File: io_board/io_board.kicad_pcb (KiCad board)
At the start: 2 copper layers, 80 x 100 mm, 83 parts, among them J10 RST1, J11 D1, J12 Osc2, J13 Rung2, J14 Sin2, J15 Gate2, J16 Ring, J18 RST2, J19 D2, J21 CV1, J22 CV2, J4 STRB1, J5 STRB2, J6 Osc1, J7 Sin1, J8 Rung1, J9 Gate1, Q1 2N3904, Q10 2N3904, Q11 2N3904, Q2 2N3904, Q5 2N3904, Q6 2N3904, Q7 2N3904, Q8 2N3904, Q9 2N3904, SW1 SW_SPDT, U3 TL074

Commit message: Routing done, panel done
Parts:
- moved R41 16.3 mm to (33.2, 41.7)
- moved Q11 9.01 mm to (41.3, 51.6), turned to 180 degrees
- moved R42 8.30 mm to (47.2, 40.6), turned to -90 degrees
- moved R49 7.82 mm to (64.1, 67.0), turned to 180 degrees
- moved R38 7.82 mm to (16.0, 67.0), turned to 0 degrees
- moved D2 6.75 mm to (58.8, 26.5)
- moved D1 6.50 mm to (18.7, 26.5)
- moved Q1 6.11 mm to (18.5, 34.1)
- moved R25 5.77 mm to (67.0, 31.9)
- moved Q2 4.86 mm to (61.5, 32.1), turned to 180 degrees
- moved R54 4.50 mm to (43.9, 1.75)
- moved R20 3.82 mm to (14.5, 30.2)
- moved D9 3.57 mm to (48.5, 19.6), turned to 90 degrees
- moved D10 3.51 mm to (48.5, 23.2), turned to -90 degrees
- moved R50 3.38 mm to (44.2, 48.2)
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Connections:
- J17 pad 3: Rst1 -> unconnected-(J17-Pad3)
- J17 pad 4: D1 -> RM
- J17 pad 5: unconnected-(J17-Pad5) -> D1
- J17 pad 6: RM -> Osc1
- J17 pad 7: Osc1 -> Rst1
- J20 pad 10: Sin2 -> Rung2
- J20 pad 11: Rung2 -> Sin2
- J20 pad 3: Rst2 -> Osc3sw
- J20 pad 5: Osc3sw -> Osc2
- J20 pad 7: Osc2 -> Clk2
- J20 pad 8: Clk2 -> QB8
- J20 pad 9: QB8 -> Rst2
- U3 pad 10: Net-(R57-Pad1) -> Net-(R58-Pad1)
- U3 pad 12: Net-(R58-Pad1) -> Net-(R57-Pad1)
- U3 pad 14: Net-(D10-Pad2) -> Net-(D9-Pad2)
- U3 pad 8: Net-(D9-Pad2) -> Net-(D10-Pad2)
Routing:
- net 12v: track 0.00 -> 286.6 mm
- net -12v: track 0.00 -> 77.9 mm
- net Rst2: track 0.00 -> 57.2 mm
- net Net-(R58-Pad1): track 0.00 -> 57.1 mm
- net Net-(R52-Pad1): track 0.00 -> 53.8 mm
- net Rst1: track 0.00 -> 52.3 mm
- net Net-(R57-Pad1): track 0.00 -> 49.2 mm
- net Net-(R51-Pad1): track 0.00 -> 46.8 mm
- net Sin2: track 0.00 -> 46.2 mm
- net Net-(J9-PadT): track 0.00 -> 45.9 mm
- net Net-(J15-PadT): track 0.00 -> 45.0 mm
- net D1: track 0.00 -> 44.9 mm
- net Osc3sw: track 0.00 -> 44.6 mm
- net Net-(FREQ1-Pad2): track 0.00 -> 44.5 mm, vias 0 -> 1
- net Net-(FREQ2-Pad2): track 0.00 -> 44.2 mm
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- added copper zone on B.Cu, net GND
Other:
- outline, holes or cut-outs redrawn

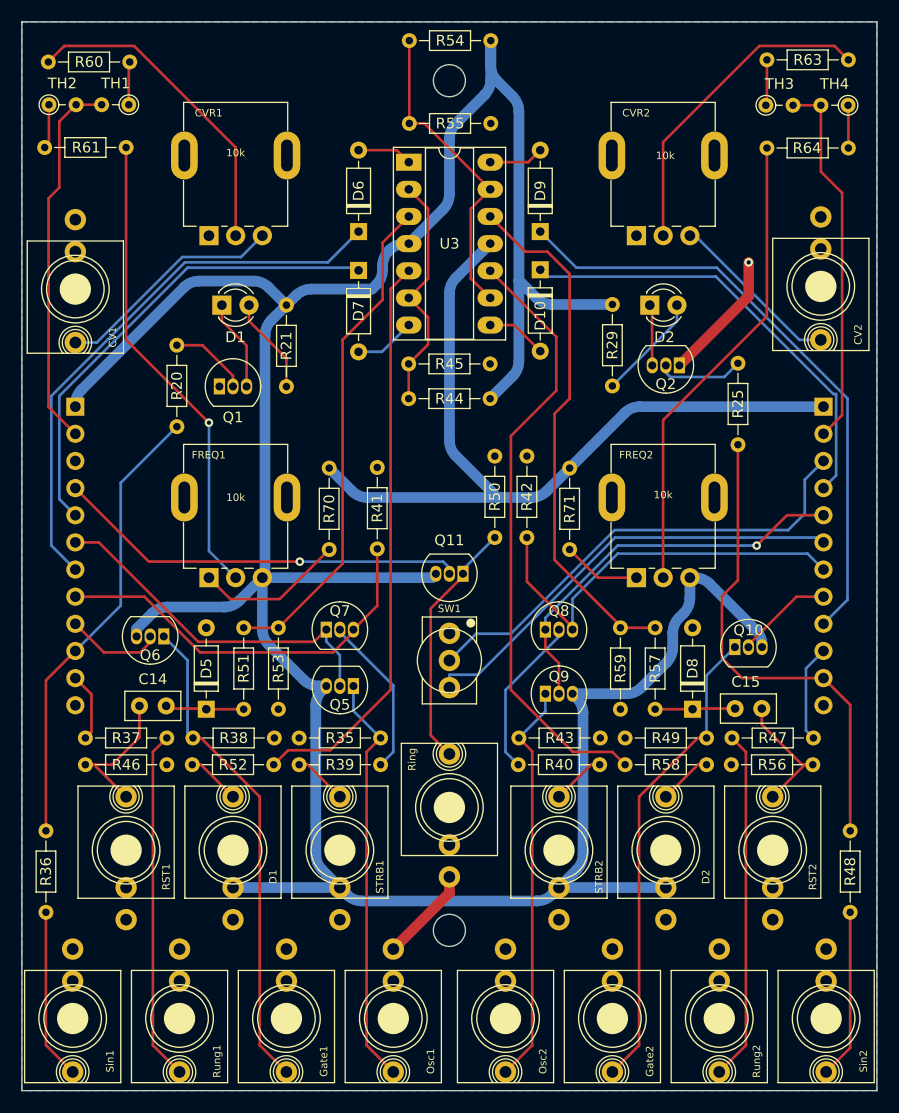
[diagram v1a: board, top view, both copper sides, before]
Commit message: Rejigged layout for more space
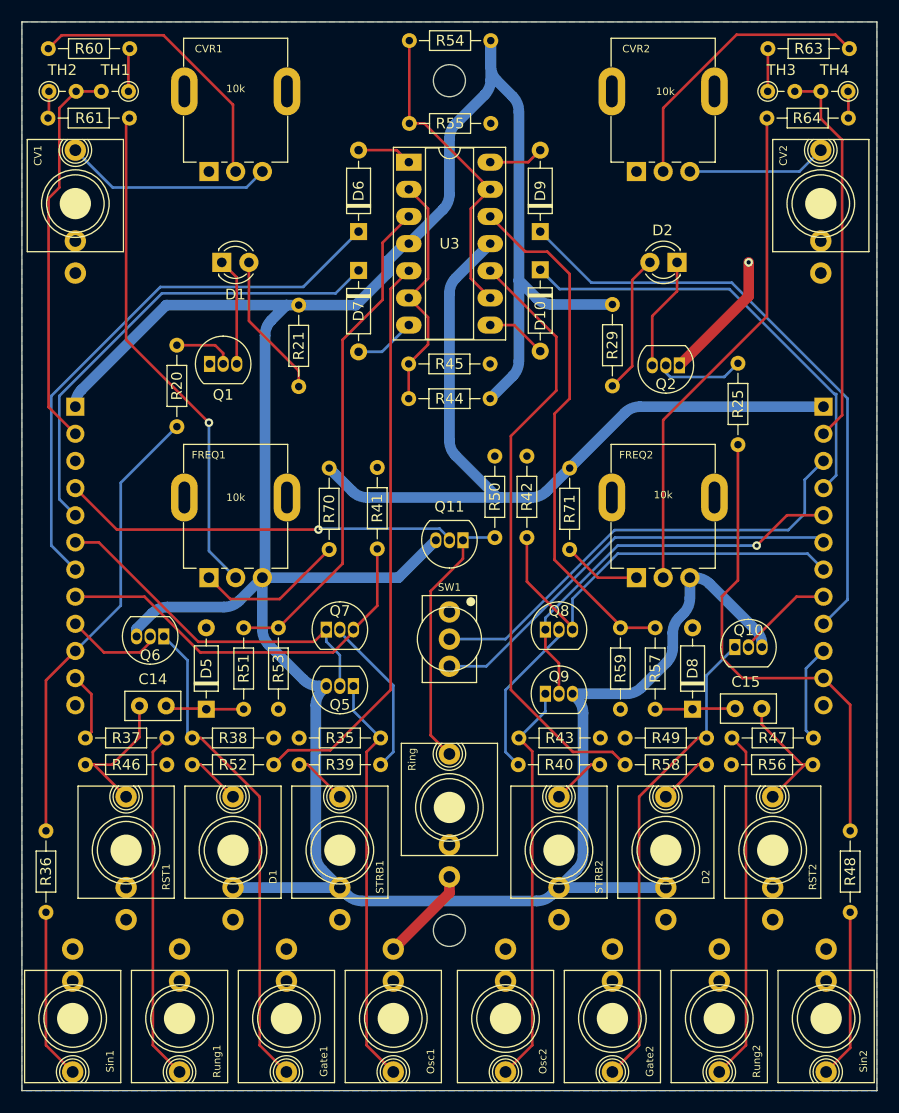
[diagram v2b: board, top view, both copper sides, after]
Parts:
- moved J21 8.00 mm to (5.00, 17.0), turned to 0 degrees
- moved J22 7.75 mm to (74.8, 17.0), turned to 0 degrees
- moved CVR1 6.00 mm to (20.0, 6.50)
- moved CVR2 6.00 mm to (60.0, 6.50)
- moved D2 4.74 mm to (61.3, 22.5), turned to 180 degrees
- moved D1 4.00 mm to (18.7, 22.5)
- moved Q11 3.14 mm to (41.3, 48.5)
- moved R64 2.80 mm to (69.7, 9.00)
- moved R61 2.77 mm to (10.1, 9.00)
- moved Q1 2.30 mm to (17.6, 32.0)
- moved SW1 2.00 mm to (40.0, 57.8)
- moved TH3 1.31 mm to (69.8, 6.50)
- moved TH4 1.30 mm to (77.3, 6.50)
- moved TH1 1.25 mm to (9.97, 6.50)
- moved R60 1.25 mm to (2.47, 2.50)
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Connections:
- CVR1 pad : (no net) -> GND
- FREQ1 pad : (no net) -> GND
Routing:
- net Net-(D2-Pad1): track 5.74 -> 10.6 mm
- net Net-(D1-Pad2): track 9.07 -> 13.6 mm
- net Net-(CVR2-Pad2): track 30.3 -> 26.7 mm
- net Net-(CVR1-Pad2): track 30.3 -> 26.7 mm
- net Net-(CVR2-Pad3): track 16.3 -> 13.1 mm
- net Net-(D2-Pad2): track 10.1 -> 13.0 mm
- net Net-(FREQ1-Pad2): track 44.5 -> 47.4 mm
- net Net-(FREQ2-Pad2): track 44.2 -> 47.0 mm
- net Net-(CVR1-Pad3): track 21.6 -> 19.6 mm
- net Net-(Q1-Pad2): track 7.43 -> 5.64 mm
- net RM: track 38.6 -> 37.0 mm
- net Net-(J16-PadT): track 23.5 -> 25.1 mm
- net Net-(R61-Pad2): track 4.17 -> 2.62 mm
- net Osc3: track 41.7 -> 40.2 mm
- net Net-(D1-Pad1): track 8.57 -> 10.1 mm
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
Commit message: Updates to panel etc.
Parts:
- added R72: 100k, Resistor_THT:R_Axial_DIN0204_L3.6mm_D1.6mm_P7.62mm_Horizontal, F.Cu at (13.5, 26.5)
- added R73: 22k, Resistor_THT:R_Axial_DIN0204_L3.6mm_D1.6mm_P7.62mm_Horizontal, F.Cu at (16.2, 17.2)
- added R74: 100k, Resistor_THT:R_Axial_DIN0204_L3.6mm_D1.6mm_P7.62mm_Horizontal, F.Cu at (53.0, 26.5)
- added R75: 22k, Resistor_THT:R_Axial_DIN0204_L3.6mm_D1.6mm_P7.62mm_Horizontal, F.Cu at (56.2, 17.2)
- moved R25 1.50 mm to (68.5, 31.9)
- moved R20 1.00 mm to (13.5, 30.2)
- moved R29 0.25 mm to (55.5, 26.4)
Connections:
- CVR1 pad : GND -> (no net)
- FREQ1 pad : GND -> (no net)
- J21 pad TN: unconnected-(J21-PadTN) -> Net-(J21-PadTN)
- J22 pad TN: unconnected-(J22-PadTN) -> Net-(J22-PadTN)
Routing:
- net Net-(J22-PadTN): track 0.00 -> 23.8 mm
- net Net-(J21-PadTN): track 0.00 -> 12.5 mm
- net Net-(Q2-Pad2): track 8.13 -> 9.63 mm
- net Net-(Q1-Pad2): track 5.64 -> 6.64 mm
- net Sin2: track 46.2 -> 46.8 mm

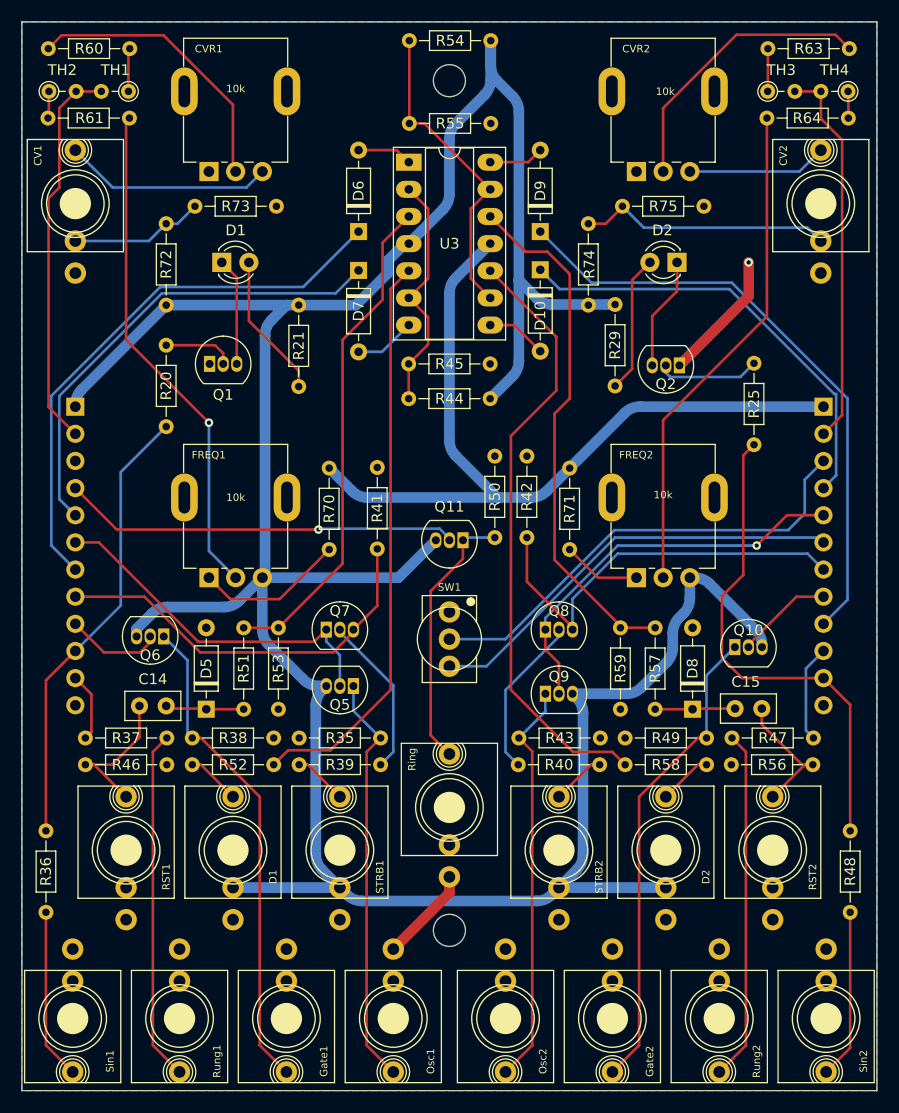
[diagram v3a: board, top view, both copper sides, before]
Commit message: Removed the unneccessary 100ohm resistor after the expo converter
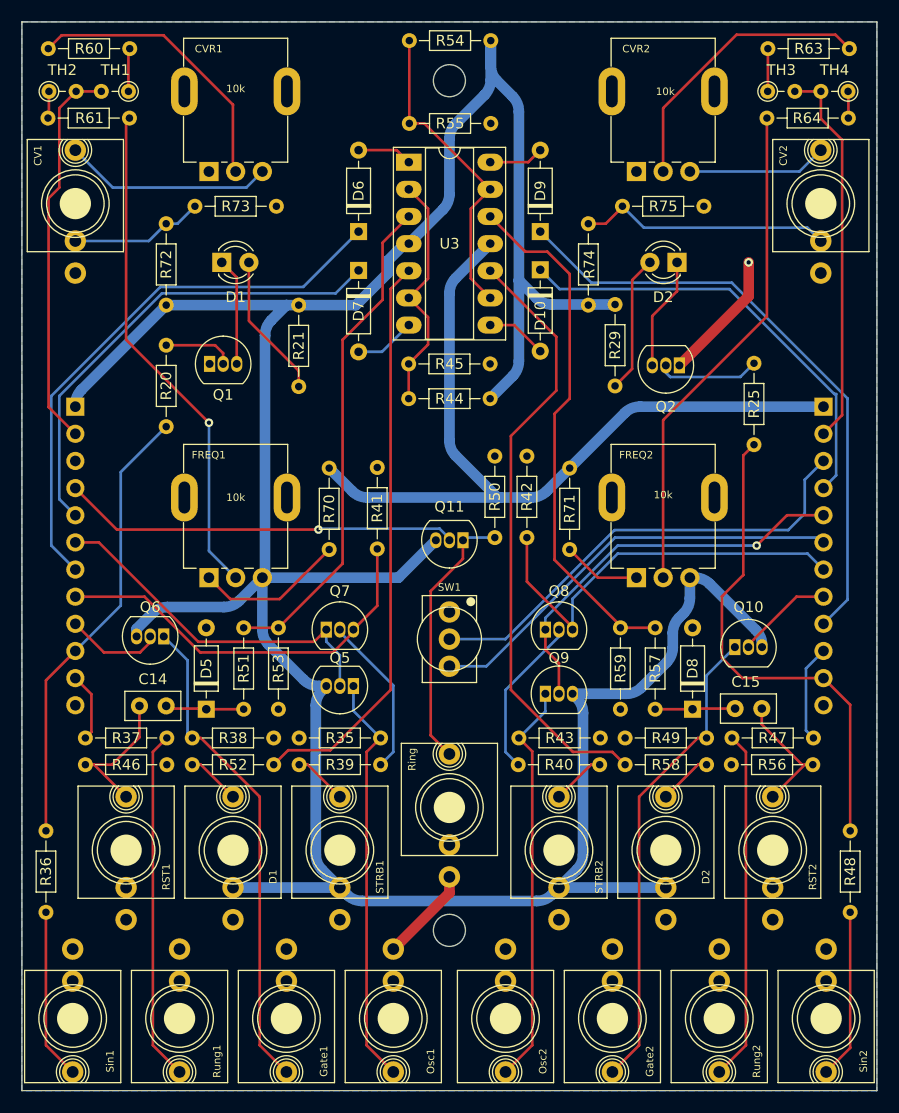
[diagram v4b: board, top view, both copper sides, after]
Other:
- board text added: "Dual Digital Sine Wave Generator Design and PCB by Neil Massey CC-BY-NC-SA 3.0 (2022) Rev 0"
- board text removed: "Design and PCB by Neil Massey CC-BY-NC-SA 3.0 (2022) Rev 0"
- board text removed: "Dual Digital Sine Wave Generator"
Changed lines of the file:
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@@
     (pad_to_mask_clearance 0)
     (pcbplotparams
-      (layerselection 0x0080000_7ffffffe)
+      (layerselection 0x00010fc_ffffffff)
       (disableapertmacros false)
-      (usegerberextensions false)
-      (usegerberattributes true)
-      (usegerberadvancedattributes true)
+      (usegerberextensions true)
+      (usegerberattributes false)
+      (usegerberadvancedattributes false)
       (creategerberjobfile true)
       (svguseinch false)
@@
       (psnegative false)
       (psa4output false)
-      (plotreference false)
+      (plotreference true)
       (plotvalue false)
       (plotinvisibletext false)
       (sketchpadsonfab false)
-      (subtractmaskfromsilk false)
-      (outputformat 3)
+      (subtractmaskfromsilk true)
+      (outputformat 1)
       (mirror false)
       (drillshape 0)
       (scaleselection 1)
-      (outputdirectory "../Assets/")
+      (outputdirectory "gerbers/")
     )
   )
@@
     (property "Sheetname" "")
     (attr through_hole)
-    (fp_text reference "Q2" (at 1.27 -1.75 180) (layer "F.SilkS")
+    (fp_text reference "Q2" (at 1.27 -3.86 180) (layer "F.SilkS")
       (effects (font (size 1 1) (thickness 0.15)))
     )
@@
     (property "Sheetname" "")
     (attr through_hole)
-    (fp_text reference "D2" (at 1.366487 3) (layer "F.SilkS")
+    (fp_text reference "D2" (at 1.3 -3.25) (layer "F.SilkS")
       (effects (font (size 1 1) (thickness 0.15)))
     )
@@
     (property "Sheetname" "")
     (attr through_hole)
-    (fp_text reference "Q10" (at 1.27 -1.58) (layer "F.SilkS")
+    (fp_text reference "Q10" (at 1.27 -3.75) (layer "F.SilkS")
       (effects (font (size 1 1) (thickness 0.15)))
     )
@@
     (property "Sheetname" "")
     (attr through_hole)
-    (fp_text reference "Q6" (at 1.27 -1.75) (layer "F.SilkS")
+    (fp_text reference "Q6" (at 1.27 2.75) (layer "F.SilkS")
       (effects (font (size 1 1) (thickness 0.15)))
     )
@@
     (property "Sheetname" "")
     (attr through_hole)
-    (fp_text reference "Q5" (at 1.27 -1.75) (layer "F.SilkS")
+    (fp_text reference "Q5" (at 1.27 2.64) (layer "F.SilkS")
       (effects (font (size 1 1) (thickness 0.15)))
     )
@@
     (property "Sheetname" "")
     (attr through_hole)
-    (fp_text reference "Q7" (at 1.27 -1.75) (layer "F.SilkS")
+    (fp_text reference "Q7" (at 1.27 -3.61) (layer "F.SilkS")
       (effects (font (size 1 1) (thickness 0.15)))
     )
@@
     (property "Sheetname" "")
     (attr through_hole)
-    (fp_text reference "D1" (at 1.3 -3) (layer "F.SilkS")
+    (fp_text reference "D1" (at 1.3 3.25) (layer "F.SilkS")
       (effects (font (size 1 1) (thickness 0.15)))
     )
@@
     (property "Sheetname" "")
     (attr through_hole)
-    (fp_text reference "Q9" (at 1.27 -1.61) (layer "F.SilkS")
+    (fp_text reference "Q9" (at 1.27 -3.36) (layer "F.SilkS")
       (effects (font (size 1 1) (thickness 0.15)))
     )
@@
     (property "Sheetname" "")
     (attr through_hole)
-    (fp_text reference "Q8" (at 1.27 -1.75) (layer "F.SilkS")
+    (fp_text reference "Q8" (at 1.27 -3.61) (layer "F.SilkS")
       (effects (font (size 1 1) (thickness 0.15)))
     )
@@
   (gr_circle (center 74.75 17) (end 77.95 17) (layer "User.2") (width 0.15) (fill none))
   (gr_circle (center 60 6.5) (end 63.6 6.5) (layer "User.2") (width 0.15) (fill none))
-  (gr_text "DDSWG" (at 40.75 49.5 90) (layer "B.SilkS")
-    (effects (font (size 20 20) (thickness 3)) (justify mirror))
+  (gr_text "DDSWG" (at 73.5 83.25 90) (layer "B.SilkS")
+    (effects (font (size 5 5) (thickness 1)) (justify mirror))
   )
-  (gr_text "Design and PCB by Neil Massey\nCC-BY-NC-SA 3.0 (2022)\nRev 0" (at 16.5 27.5 90) (layer "B.SilkS")
-    (effects (font (size 2 2) (thickness 0.4)) (justify mirror))
-  )
-  (gr_text "Dual Digital Sine Wave Generator" (at 69.5 50 90) (layer "B.SilkS")
-    (effects (font (size 3.5 3.5) (thickness 0.5)) (justify mirror))
+  (gr_text "Dual Digital Sine Wave Generator\nDesign and PCB by Neil Massey\nCC-BY-NC-SA 3.0 (2022)\nRev 0" (at 7.5 83.5 90) (layer "B.SilkS")
+    (effects (font (size 1.2 1.2) (thickness 0.2)) (justify mirror))
   )
   (segment (start 13.5 64.25) (end 17.19 64.25) (width 0.25) (layer "F.Cu") (net 1))

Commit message: Added negative CV protection diodes
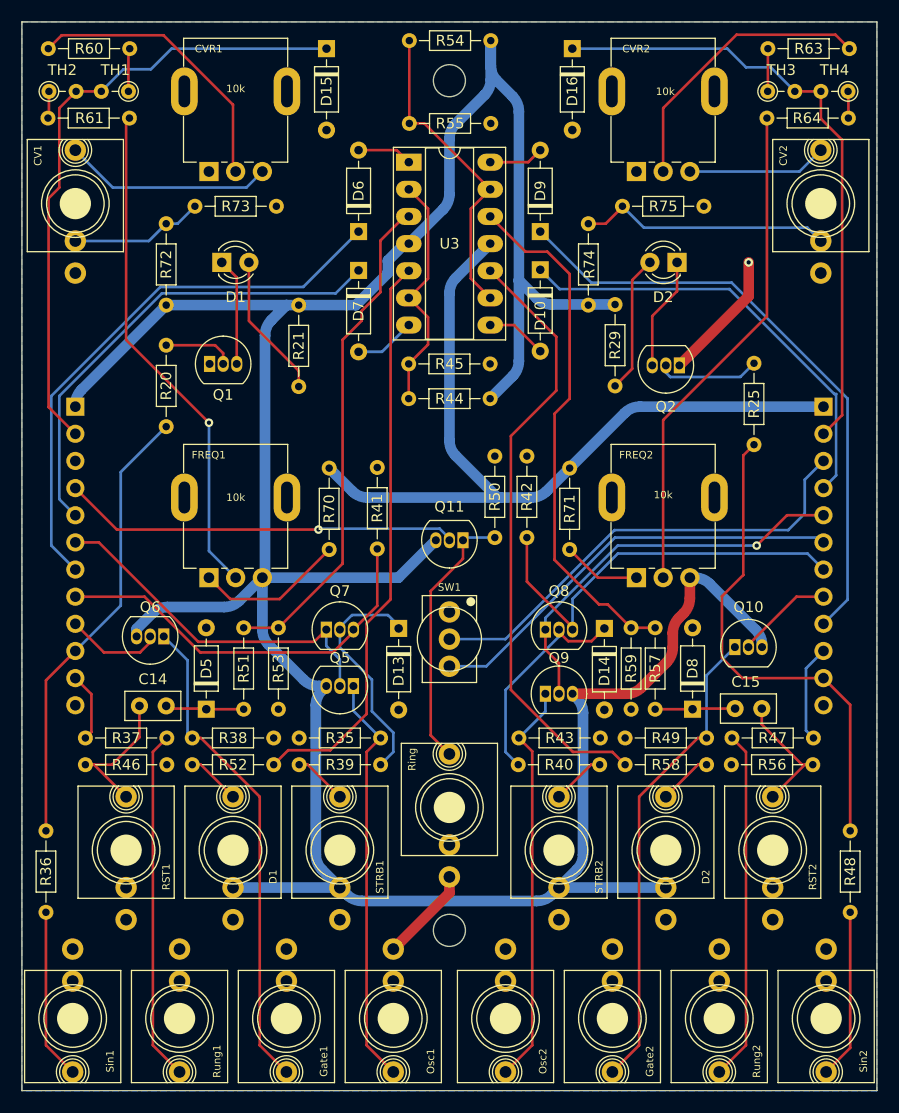
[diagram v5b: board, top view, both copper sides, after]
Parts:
- added D13: BAT42, Diode_THT:D_DO-35_SOD27_P7.62mm_Horizontal, F.Cu at (35.2, 56.8)
- added D14: BAT42, Diode_THT:D_DO-35_SOD27_P7.62mm_Horizontal, F.Cu at (54.5, 56.8)
- added D15: BAT42, Diode_THT:D_DO-35_SOD27_P7.62mm_Horizontal, F.Cu at (28.5, 2.50)
- added D16: BAT42, Diode_THT:D_DO-35_SOD27_P7.62mm_Horizontal, F.Cu at (51.5, 2.50)
- moved R59 1.00 mm to (57.0, 56.7)
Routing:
- net CV1: track 36.5 -> 59.2 mm
- net CV2: track 36.0 -> 58.5 mm
- net Net-(D13-Pad1): track 15.2 -> 22.1 mm
- net Net-(D14-Pad1): track 15.2 -> 20.5 mm

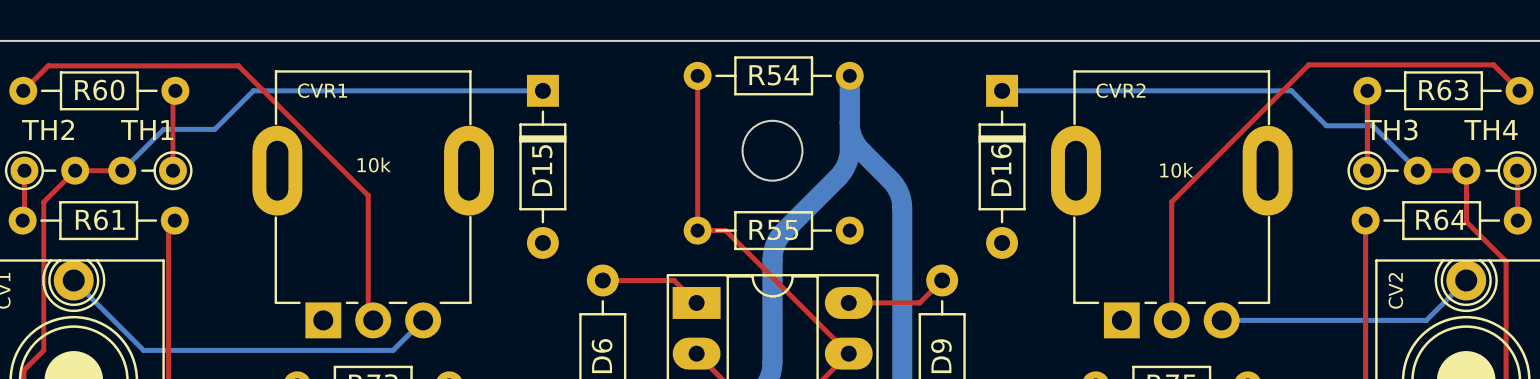
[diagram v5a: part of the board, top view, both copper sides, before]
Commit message: Flip flop on CV protection diodes
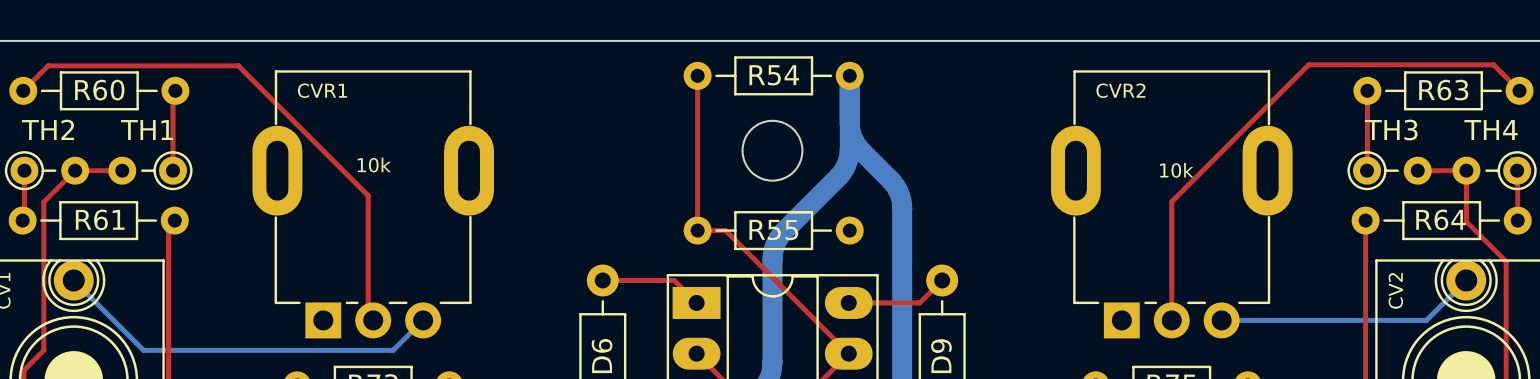
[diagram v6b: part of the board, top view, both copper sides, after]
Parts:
- removed D15, D16: BAT42, Diode_THT:D_DO-35_SOD27_P7.62mm_Horizontal
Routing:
- net CV1: track 59.2 -> 36.5 mm
- net CV2: track 58.5 -> 36.0 mm
